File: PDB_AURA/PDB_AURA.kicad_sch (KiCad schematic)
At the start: 0 parts

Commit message: Moving to laptop
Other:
- sheet 200_Connectors renamed 300_Connectors
- added sheet 200_Buck_Regulator (Buck_Regulator.kicad_sch)
- note removed: "5V, PWM"
- note removed: "PCB"
- note removed: "Project Block Diagram"
- note removed: "Servo Motors"
- note removed: "USB or Battery (7V2 -> 16V8)"
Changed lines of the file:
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@@
-		)
-	)
-	(rectangle
-		(start 27.305 95.25)
-		(end 52.07 120.65)
-		(stroke
-			(width 0)
-			(type solid)
-		)
-		(fill
-			(type none)
-		)
-	)
-	(rectangle
-		(start 59.055 44.45)
-		(end 101.6 127)
-		(stroke
-			(width 0)
-			(type default)
-		)
-		(fill
-			(type none)
-		)
-	)
-	(rectangle
-		(start 27.94 50.8)
-		(end 52.705 76.2)
-		(stroke
-			(width 0)
-			(type solid)
-		)
-		(fill
-			(type none)
 		)
 	)
@@
 		)
 	)
-	(text "PCB"
-		(exclude_from_sim no)
-		(at 59.055 43.18 0)
-		(effects
-			(font
-				(size 1.27 1.27)
-			)
-			(justify left)
-		)
-	)
-	(text "5V, PWM"
-		(exclude_from_sim no)
-		(at 59.69 62.484 0)
-		(effects
-			(font
-				(size 1.27 1.27)
-			)
-		)
-	)
 	(text "Maybe switch regulator to SiC437/SiC431.\n\nConfirm power specifications.\n\nFix block diagram (it is outdated)."
 		(exclude_from_sim no)
@@
 			)
 			(justify left top)
-		)
-	)
-	(text "Project Block Diagram\n"
-		(exclude_from_sim no)
-		(at 27.94 32.004 0)
-		(effects
-			(font
-				(size 2.54 2.54)
-				(thickness 0.508)
-				(bold yes)
-			)
-			(justify left)
-		)
-	)
-	(text "USB or Battery (7V2 -> 16V8)\n"
-		(exclude_from_sim no)
-		(at 40.386 93.98 0)
-		(effects
-			(font
-				(size 1.27 1.27)
-			)
 		)
 	)
@@
 			)
 			(justify left)
-		)
-	)
-	(text "Servo Motors"
-		(exclude_from_sim no)
-		(at 27.94 49.53 0)
-		(effects
-			(font
-				(size 1.27 1.27)
-			)
-			(justify left)
-		)
-	)
-	(polyline
-		(pts
-			(xy 40.64 63.5) (xy 43.18 61.595)
-		)
-		(stroke
-			(width 0.635)
-			(type solid)
-		)
-	)
-	(polyline
-		(pts
-			(xy 78.74 69.85) (xy 76.835 72.39)
-		)
-		(stroke
-			(width 0.635)
-			(type solid)
-		)
-	)
-	(polyline
-		(pts
-			(xy 72.39 107.95) (xy 69.85 109.855)
-		)
-		(stroke
-			(width 0.635)
-			(type solid)
-		)
-	)
-	(polyline
-		(pts
-			(xy 78.74 79.375) (xy 78.74 101.6)
-		)
-		(stroke
-			(width 0.635)
-			(type solid)
-		)
-	)
-	(polyline
-		(pts
-			(xy 46.99 107.95) (xy 71.755 107.95)
-		)
-		(stroke
-			(width 0.635)
-			(type solid)
-		)
-	)
-	(polyline
-		(pts
-			(xy 40.64 63.5) (xy 72.39 63.5)
-		)
-		(stroke
-			(width 0.635)
-			(type solid)
-		)
-	)
-	(polyline
-		(pts
-			(xy 40.64 63.5) (xy 43.18 65.405)
-		)
-		(stroke
-			(width 0.635)
-			(type solid)
-		)
-	)
-	(polyline
-		(pts
-			(xy 78.74 69.85) (xy 78.74 75.565)
-		)
-		(stroke
-			(width 0.635)
-			(type solid)
-		)
-	)
-	(polyline
-		(pts
-			(xy 72.39 107.95) (xy 69.85 106.045)
-		)
-		(stroke
-			(width 0.635)
-			(type solid)
-		)
-	)
-	(polyline
-		(pts
-			(xy 78.74 69.85) (xy 80.645 72.39)
-		)
-		(stroke
-			(width 0.635)
-			(type solid)
 		)
 	)
@@
 			(color 0 0 0 0.0000)
 		)
-		(property "Sheetname" "200_Connectors"
+		(property "Sheetname" "300_Connectors"
 			(at 65.405 50.0884 0)
 			(effects
@@
 			(project "PDB_AURA"
 				(path "/c0b09de1-c640-438f-9ef5-dda14a6aac71"
-					(page "3")
+					(page "4")
 				)
 			)
@@
 				)
 			)
+		)
+	)
+	(sheet
+		(at 101.6 76.2)
+		(size 25.4 25.4)
+		(exclude_from_sim no)
+		(in_bom yes)
+		(on_board yes)
+		(dnp no)
+		(fields_autoplaced yes)
+		(stroke
+			(width 0.1524)
+			(type solid)
+		)
+		(fill
+			(color 0 0 0 0.0000)
+		)
+		(property "Sheetname" "200_Buck_Regulator"
+			(at 101.6 75.4884 0)
+			(effects
+				(font
+					(size 1.27 1.27)
+				)
+				(justify left bottom)
+			)
+		)
+		(property "Sheetfile" "Buck_Regulator.kicad_sch"
+			(at 101.6 102.1846 0)
+			(effects
+				(font
+					(size 1.27 1.27)
+				)
+				(justify left top)
+			)
+		)
+		(instances
+			(project "PDB_AURA"
+				(path "/c0b09de1-c640-438f-9ef5-dda14a6aac71"
+					(page "3")
+				)
+			)

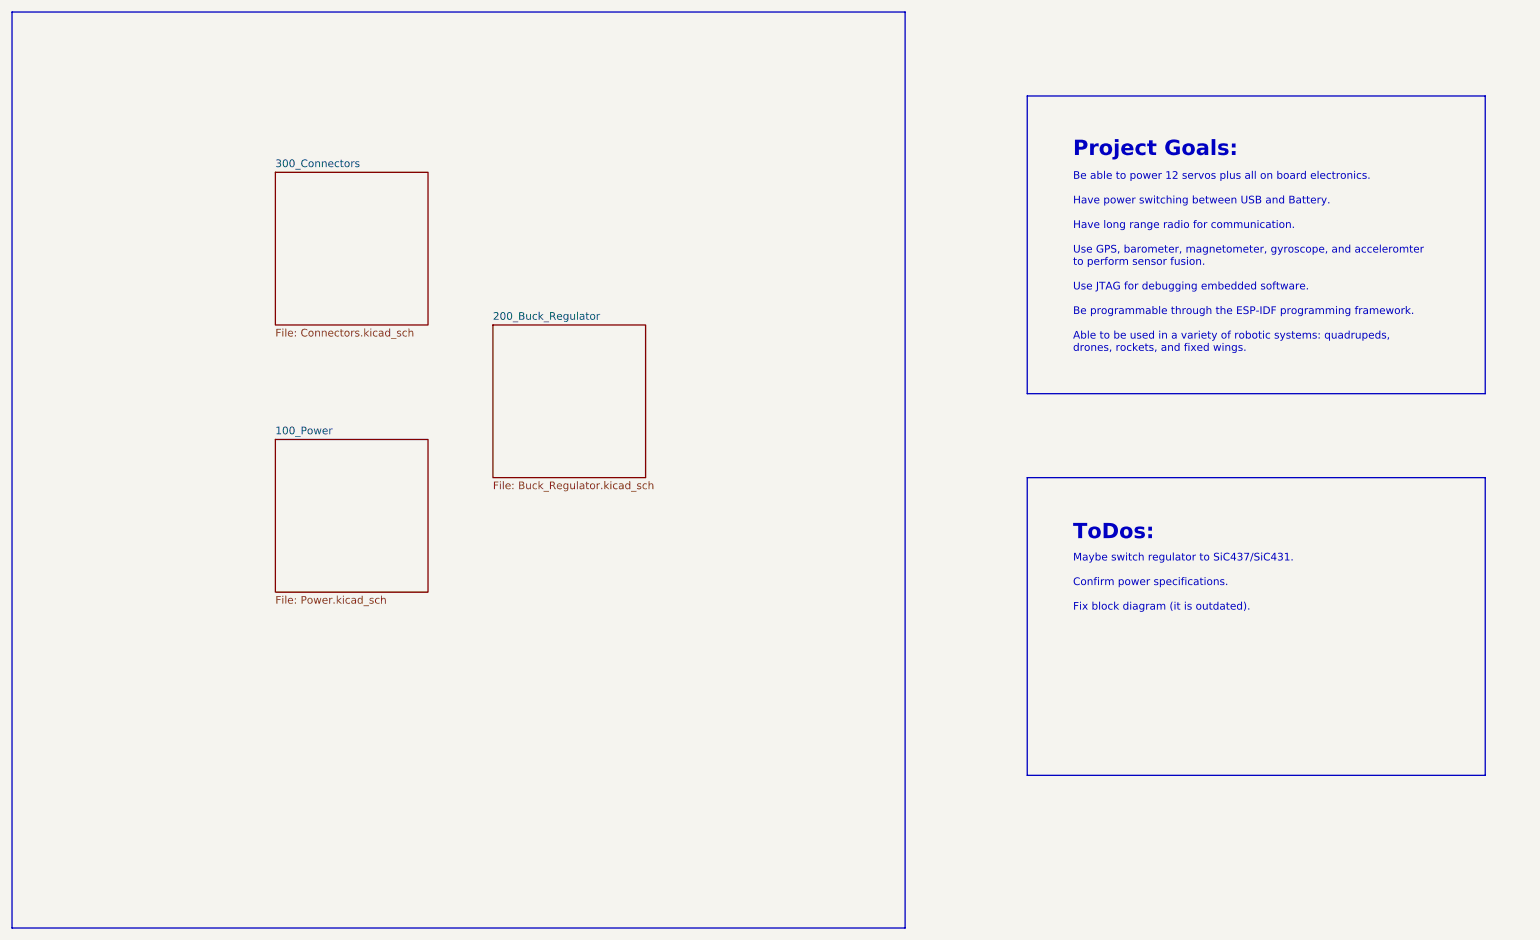
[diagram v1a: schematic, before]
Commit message: Synchronised project outline and block diagram
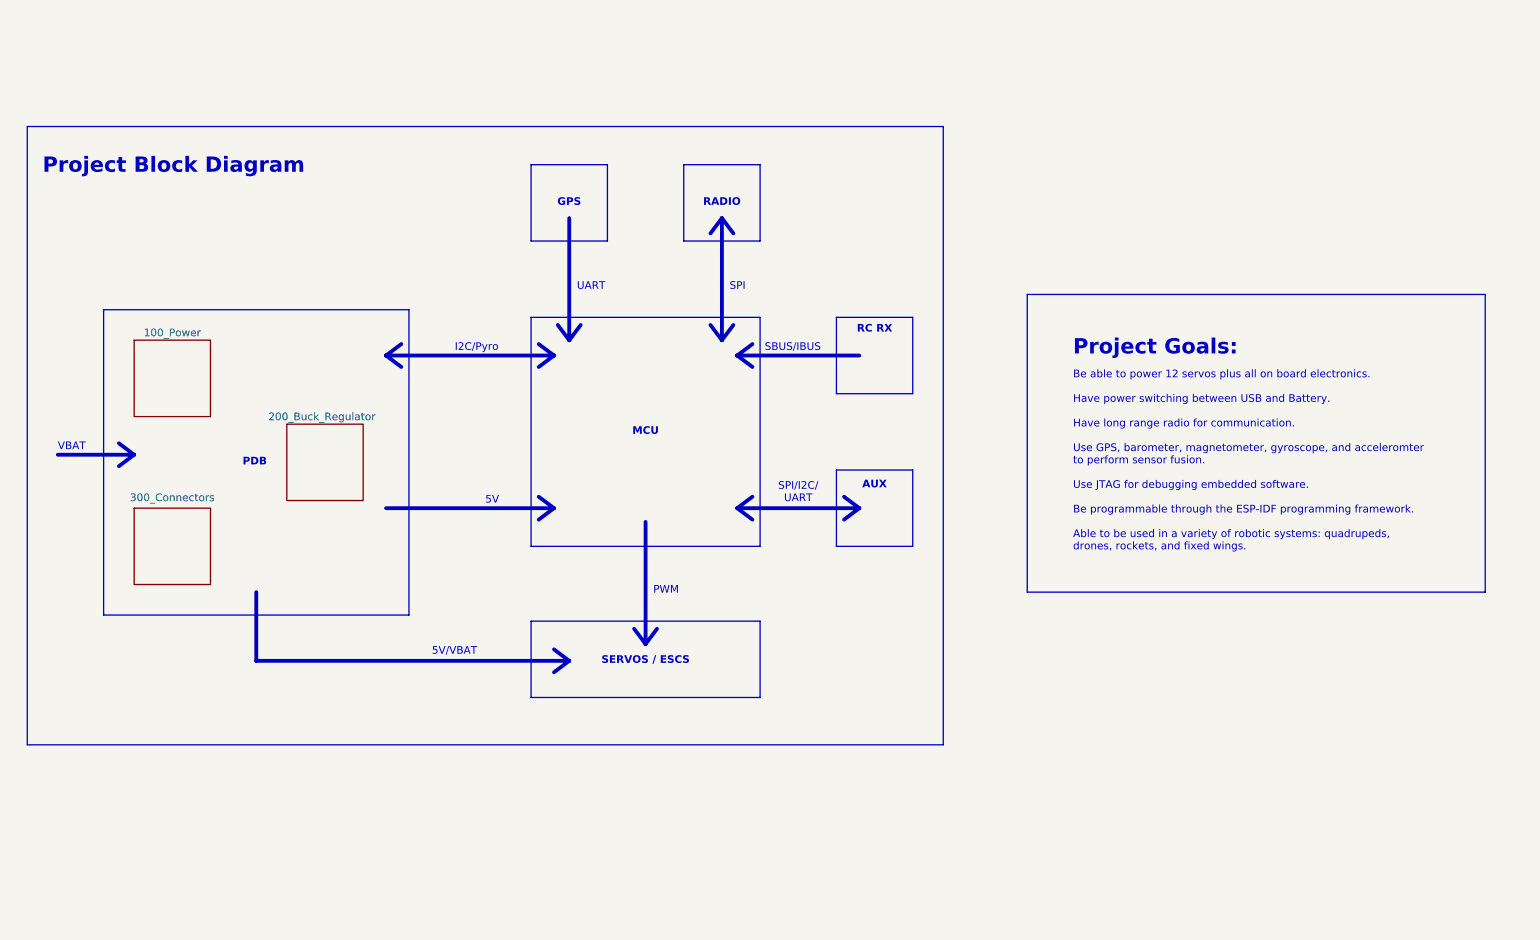
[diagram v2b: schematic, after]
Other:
- note added: "5V"
- note added: "5V/VBAT"
- note added: "AUX"
- note added: "GPS"
- note added: "I2C/Pyro"
- note added: "MCU"
- note added: "PDB"
- note added: "PWM"
- note added: "Project Block Diagram"
- note added: "RADIO"
- note added: "RC RX"
- note added: "SBUS/IBUS"
- note added: "SERVOS / ESCS"
- note added: "SPI"
- note added: "SPI/I2C/ UART"
- note added: "UART"
- note added: "VBAT"
- note removed: "Maybe switch regulator to SiC437/SiC431. Confirm power specifications. Fix block diagram (it is outdated)."
- note removed: "ToDos:"
